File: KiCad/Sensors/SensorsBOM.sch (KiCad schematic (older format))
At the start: 9 parts, among them J1 BERG 2x6, U1 OPA1641

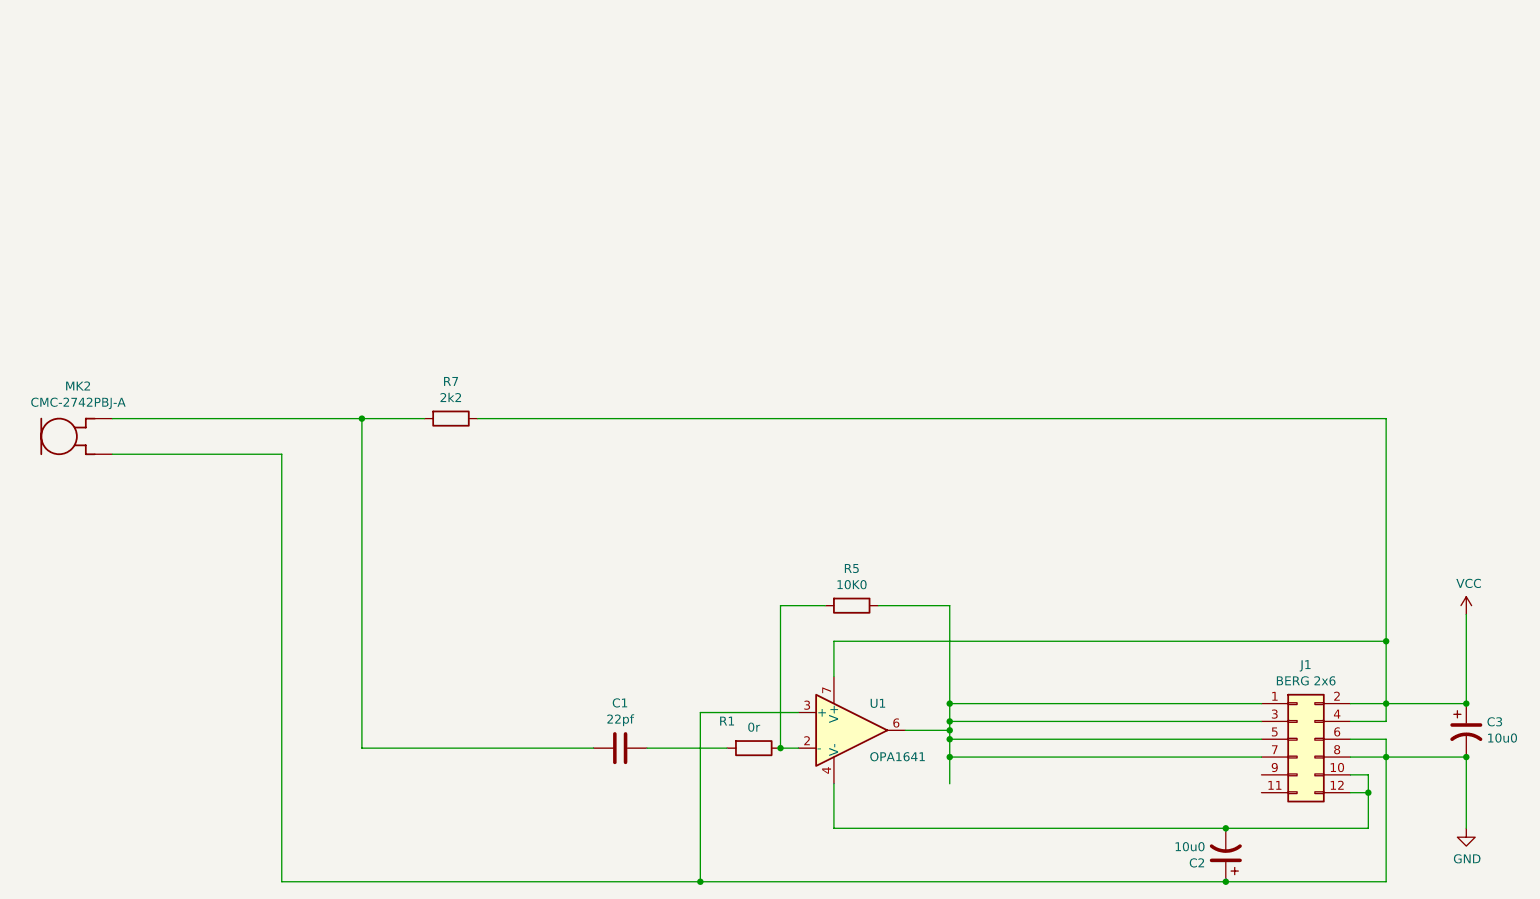
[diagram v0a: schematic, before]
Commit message: Changed to I2C Temperature Sensor
The older RTD temperature sensor was replaced by an I2C one located on the main board.

This also brough in changes to the sensor module and additional data on the JSON shot info
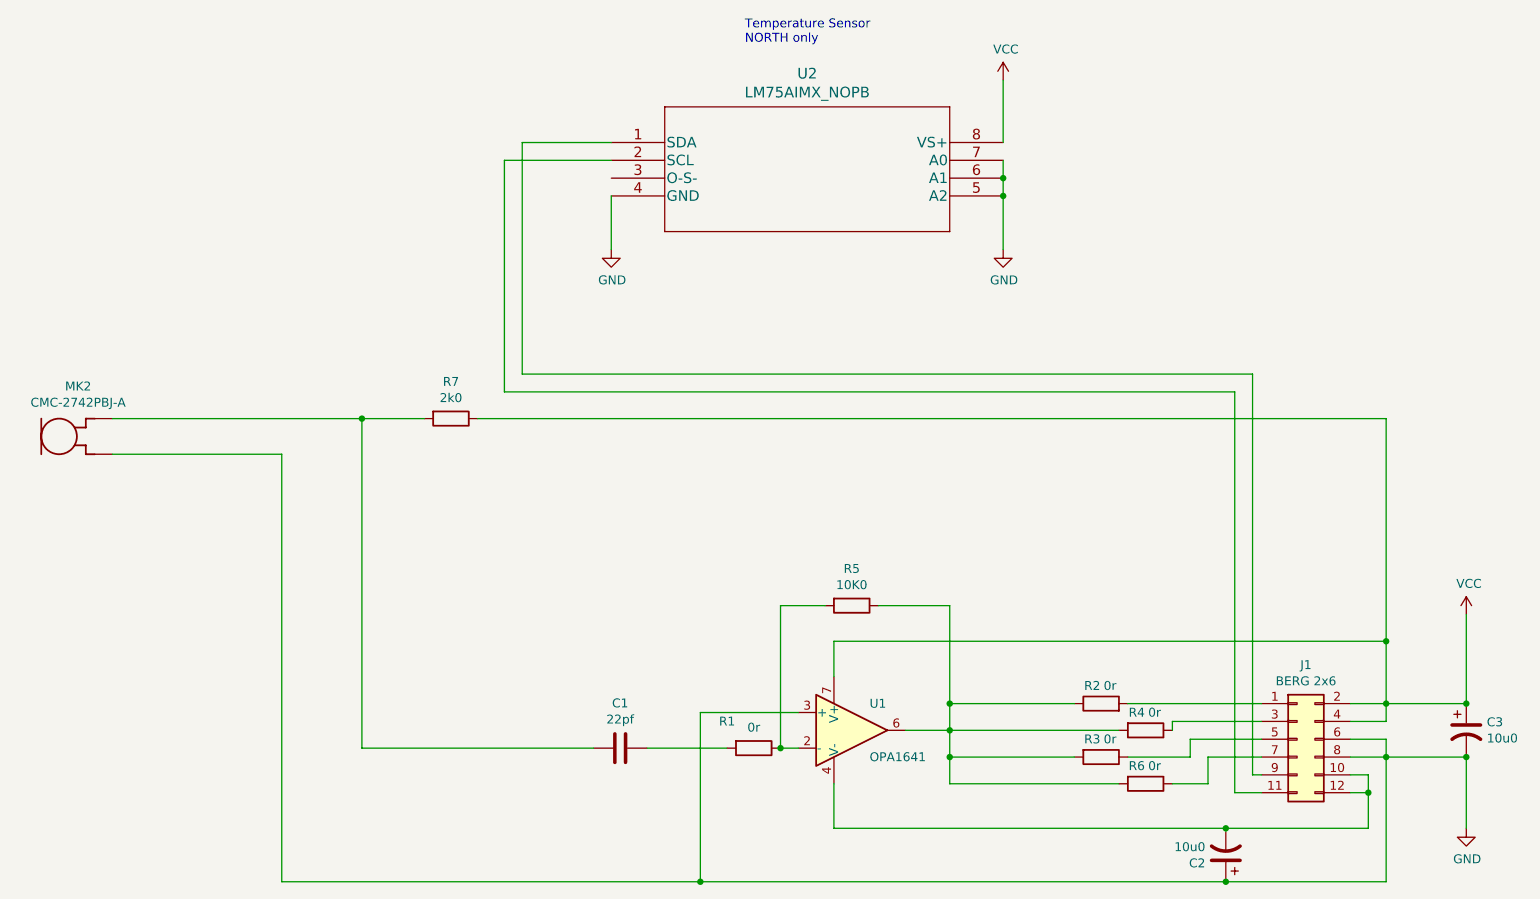
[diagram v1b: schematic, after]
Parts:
- added R2, R3, R4, R6: 0r, Resistor_SMD:R_0805_2012Metric, symbol Device:R
- added U2: LM75AIMX_NOPB, Package_SO:SOIC-8-1EP_3.9x4.9mm_P1.27mm_EP2.29x3mm, symbol 2020-05-12_18-19-55:LM75AIMX_NOPB
- C1: DigiKey (none) -> 399-1113-ND
- C2: DigiKey (none) -> 396-3684-1-ND
- C3: DigiKey (none) -> 399-3684-1-ND
- MK2: DigiKey (none) -> 192-1726-ND; Field4 Manufacturer recommendations -> (none)
- R1, R5: DigiKey (none) -> 311-0.0ARCT-ND
- R7: value 2k2 -> 2k0; DigiKey (none) -> 311-00KCRCT-ND
- U1: DigiKey (none) -> 296-48624-1-ND
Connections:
- net GND: now also U2.4 (GND), U2.5 (A2), U2.6 (A1), U2.7 (A0)
- net VCC: now also U2.8 (VS+)
- net at J1.11 (Pin_11): now also U2.2 (SCL)
- net at J1.9 (Pin_9): now also U2.1 (SDA)
- new net: R2.1, R3.2, R4.2, R5.1, R6.2, U1.6
- new net: J1.3 (Pin_3), R4.1
- new net: J1.5 (Pin_5), R3.1
- new net: J1.7 (Pin_7), R6.1
- new net: J1.1 (Pin_1), R2.2
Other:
- note added: "Temperature Sensor\nNORTH only"
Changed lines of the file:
@@
 F 2 "Resistor_SMD:R_0805_2012Metric" H 5438 4750 50  0001 C CNN
 F 3 "~" H 5400 4900 50  0001 C CNN
+F 4 "399-1113-ND" V 5400 4900 50  0001 C CNN "DigiKey"
 	1    5400 4900
 	0    1    1    0
@@
 F 2 "Resistor_SMD:R_0805_2012Metric" V 6630 4100 50  0001 C CNN
 F 3 "~" H 6700 4100 50  0001 C CNN
+F 4 "311-0.0ARCT-ND" V 6700 4100 50  0001 C CNN "DigiKey"
 	1    6700 4100
 	0    1    1    0
 $EndComp
 Wire Wire Line
-	7250 4800 7250 4750
+	7250 4800 7250 4650
 Wire Wire Line
 	7250 4100 6850 4100
@@
 Wire Wire Line
 	6400 4900 6300 4900
+$Comp
+L Device:R R4
+U 1 1 5E6F20B4
+P 8350 4800
+F 0 "R4" V 8250 4750 50  0000 C CNN
+F 1 "0r" V 8250 4850 50  0000 C CNN
+F 2 "Resistor_SMD:R_0805_2012Metric" V 8280 4800 50  0001 C CNN
+F 3 "~" H 8350 4800 50  0001 C CNN
+F 4 "311-0.0ARCT-ND" V 8350 4800 50  0001 C CNN "DigiKey"
+	1    8350 4800
+	0    1    1    0
+$EndComp
+$Comp
+L Device:R R3
+U 1 1 5E6F2C35
+P 8100 4950
+F 0 "R3" V 8000 4900 50  0000 C CNN
+F 1 "0r" V 8000 5000 50  0000 C CNN
+F 2 "Resistor_SMD:R_0805_2012Metric" V 8030 4950 50  0001 C CNN
+F 3 "~" H 8100 4950 50  0001 C CNN
+F 4 "311-0.0ARCT-ND" V 8100 4950 50  0001 C CNN "DigiKey"
+	1    8100 4950
+	0    1    1    0
+$EndComp
+$Comp
+L Device:R R6
+U 1 1 5E6F34FA
+P 8350 5100
+F 0 "R6" V 8250 5050 50  0000 C CNN
+F 1 "0r" V 8250 5150 50  0000 C CNN
+F 2 "Resistor_SMD:R_0805_2012Metric" V 8280 5100 50  0001 C CNN
+F 3 "~" H 8350 5100 50  0001 C CNN
+F 4 "311-0.0ARCT-ND" V 8350 5100 50  0001 C CNN "DigiKey"
+	1    8350 5100
+	0    1    1    0
+$EndComp
+$Comp
+L Device:R R2
+U 1 1 5E6F39DE
+P 8100 4650
+F 0 "R2" V 8200 4700 50  0000 C CNN
+F 1 "0r" V 8200 4600 50  0000 C CNN
+F 2 "Resistor_SMD:R_0805_2012Metric" V 8030 4650 50  0001 C CNN
+F 3 "~" H 8100 4650 50  0001 C CNN
+F 4 "311-0.0ARCT-ND" V 8100 4650 50  0001 C CNN "DigiKey"
+	1    8100 4650
+	0    -1   -1   0
+$EndComp
+Wire Wire Line
+	7950 4650 7250 4650
 Connection ~ 7250 4650
 Wire Wire Line
 	7250 4650 7250 4100
+Wire Wire Line
+	8200 4800 7250 4800
 Connection ~ 7250 4800
 Wire Wire Line
-	7250 4950 7250 4850
+	7250 4950 7250 4800
+Wire Wire Line
+	8200 5100 7250 5100
 Wire Wire Line
 	7250 5100 7250 4950
 Connection ~ 7250 4950
+Wire Wire Line
+	7250 4950 7950 4950
+Wire Wire Line
+	8250 4650 9000 4650
+Wire Wire Line
+	9000 4750 8500 4750
+Wire Wire Line
+	8500 4750 8500 4800
+Wire Wire Line
+	8600 4950 8600 4850
+Wire Wire Line
+	8600 4850 9000 4850
+Wire Wire Line
+	8250 4950 8600 4950
+Wire Wire Line
+	8500 5100 8700 5100
+Wire Wire Line
+	8700 5100 8700 4950
+Wire Wire Line
+	8700 4950 9000 4950
 Wire Wire Line
 	6600 4300 6600 4500
@@
 F 2 "Resistor_SMD:R_1206_3216Metric" H 10150 4800 50  0001 C CNN
 F 3 "~" H 10150 4800 50  0001 C CNN
+F 4 "399-3684-1-ND" H 10150 4800 50  0001 C CNN "DigiKey"
 	1    10150 4800
 	1    0    0    -1
@@
 F 2 "Resistor_SMD:R_1206_3216Metric" H 8800 5500 50  0001 C CNN
 F 3 "~" H 8800 5500 50  0001 C CNN
+F 4 "396-3684-1-ND" H 8800 5500 50  0001 C CNN "DigiKey"
 	1    8800 5500
 	-1   0    0    1
@@
 P 4450 3050
 F 0 "R7" V 4243 3050 50  0000 C CNN
-F 1 "2k2" V 4334 3050 50  0000 C CNN
+F 1 "2k0" V 4334 3050 50  0000 C CNN
 F 2 "Resistor_SMD:R_0805_2012Metric" V 4380 3050 50  0001 C CNN
 F 3 "~" H 4450 3050 50  0001 C CNN
+F 4 "311-00KCRCT-ND" V 4450 3050 50  0001 C CNN "DigiKey"
 	1    4450 3050
 	0    1    1    0
@@
 F 2 "CUI_CMC-2742PBJ-A" H 2250 3150 50  0001 L BNN
 F 3 "CUI INC" H 2250 3150 50  0001 L BNN
-F 4 "Manufacturer recommendations" H 2250 3150 50  0001 L BNN "Field4"
+F 4 "192-1726-ND" H 2250 3150 50  0001 L BNN "DigiKey"
+F 5 "" H 2250 3150 50  0001 C CNN "Field5"
 	1    2250 3150
 	1    0    0    -1
@@
 	1    0    0    -1
 $EndComp
+Text Notes 6100 950  0    50   ~ 0
+Temperature Sensor\nNORTH only
 Wire Wire Line
 	2550 3050 3950 3050
@@
 F 2 "Package_SO:SOIC-8-1EP_3.9x4.9mm_P1.27mm_EP2.29x3mm" H 6700 4800 50  0001 C CNN
 F 3 "http://www.ti.com/lit/ds/symlink/opa1641.pdf" H 6700 4800 50  0001 C CNN
+F 4 "296-48624-1-ND" H 6700 4800 50  0001 C CNN "DigiKey"
 	1    6700 4800
 	1    0    0    -1
@@
 F 2 "Resistor_SMD:R_0805_2012Metric" V 6080 4900 50  0001 C CNN
 F 3 "~" H 6150 4900 50  0001 C CNN
+F 4 "311-0.0ARCT-ND" V 6150 4900 50  0001 C CNN "DigiKey"
 	1    6150 4900
 	0    1    1    0
@@
 	9600 5150 9600 5350
 Wire Wire Line
+	8950 5050 9000 5050
+Wire Wire Line
 	9700 4950 10150 4950
 Connection ~ 10150 4950
+$Comp
+L 2020-05-12_18-19-55:LM75AIMX_NOPB U2
+U 1 1 5EFCD1FE
+P 5350 1500
+F 0 "U2" H 6450 1887 60  0000 C CNN
+F 1 "LM75AIMX_NOPB" H 6450 1781 60  0000 C CNN
+F 2 "Package_SO:SOIC-8-1EP_3.9x4.9mm_P1.27mm_EP2.29x3mm" H 6450 1740 60  0001 C CNN
+F 3 "" H 5350 1500 60  0000 C CNN
+F 4 "LM75AIMX/NOP8CT-ND" H 5350 1500 50  0001 C CNN "DigiKey"
+	1    5350 1500
+	1    0    0    -1
+$EndComp
+Wire Wire Line
+	7550 1600 7550 1700
+Connection ~ 7550 1700
+Wire Wire Line
+	7550 1700 7550 1800
+$Comp
+L power:GND #PWR01
+U 1 1 5EFD16B7
+P 5350 2100
+F 0 "#PWR01" H 5350 1850 50  0001 C CNN
+F 1 "GND" H 5355 1927 50  0000 C CNN
+F 2 "" H 5350 2100 50  0001 C CNN
+F 3 "" H 5350 2100 50  0001 C CNN
+	1    5350 2100
+	1    0    0    -1
+$EndComp
+Wire Wire Line
+	5350 1800 5350 2100
+Wire Wire Line
+	4850 2800 4850 1500
+Wire Wire Line
+	9000 5150 8850 5150
+Wire Wire Line
+	4750 2900 4750 1600
+Wire Wire Line
+	4750 1600 5350 1600
 Wire Wire Line
 	4600 3050 9700 3050
-Wire Wire Line
-	7250 4650 9000 4650
-Wire Wire Line
-	7250 4750 9000 4750
-Connection ~ 7250 4750
-Wire Wire Line
-	7250 4750 7250 4650
-Wire Wire Line
-	7250 4850 9000 4850
-Connection ~ 7250 4850
-Wire Wire Line
-	7250 4850 7250 4800
-Wire Wire Line
-	7250 4950 9000 4950
+$Comp
+L power:GND #PWR0103
+U 1 1 5EFDF253
+P 7550 2100
+F 0 "#PWR0103" H 7550 1850 50  0001 C CNN
+F 1 "GND" H 7555 1927 50  0000 C CNN
+F 2 "" H 7550 2100 50  0001 C CNN
+F 3 "" H 7550 2100 50  0001 C CNN
+	1    7550 2100
+	1    0    0    -1
+$EndComp
+Wire Wire Line
+	7550 2100 7550 1800
+Connection ~ 7550 1800
+$Comp
+L power:VCC #PWR0104
+U 1 1 5EFE1497
+P 7550 1150
+F 0 "#PWR0104" H 7550 1000 50  0001 C CNN
+F 1 "VCC" H 7565 1323 50  0000 C CNN
+F 2 "" H 7550 1150 50  0001 C CNN
+F 3 "" H 7550 1150 50  0001 C CNN
+	1    7550 1150
+	1    0    0    -1
+$EndComp
+Wire Wire Line
+	7550 1150 7550 1500
+Wire Wire Line
+	5350 1500 4850 1500
+Wire Wire Line
+	4850 2800 8950 2800
+Wire Wire Line
+	8950 2800 8950 5050
+Wire Wire Line
+	4750 2900 8850 2900
+Wire Wire Line
+	8850 2900 8850 5150
 $EndSCHEMATC
